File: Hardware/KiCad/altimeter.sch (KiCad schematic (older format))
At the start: 16 parts

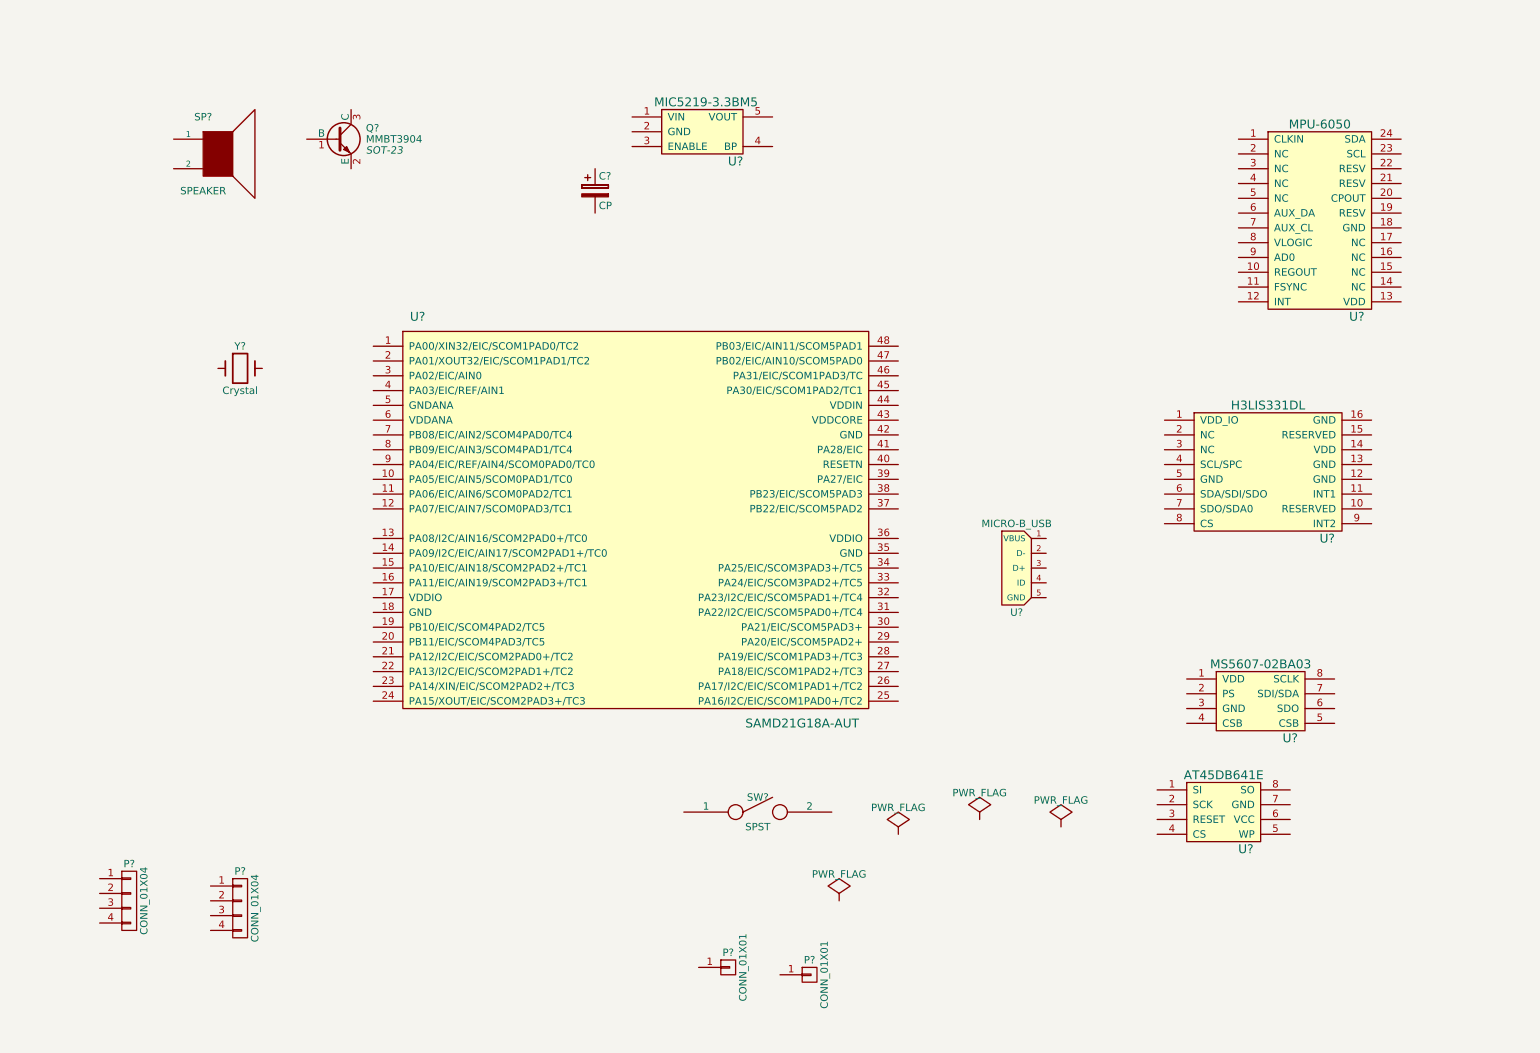
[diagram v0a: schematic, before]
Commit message: Pyro output, regulator and buzzer schematics created
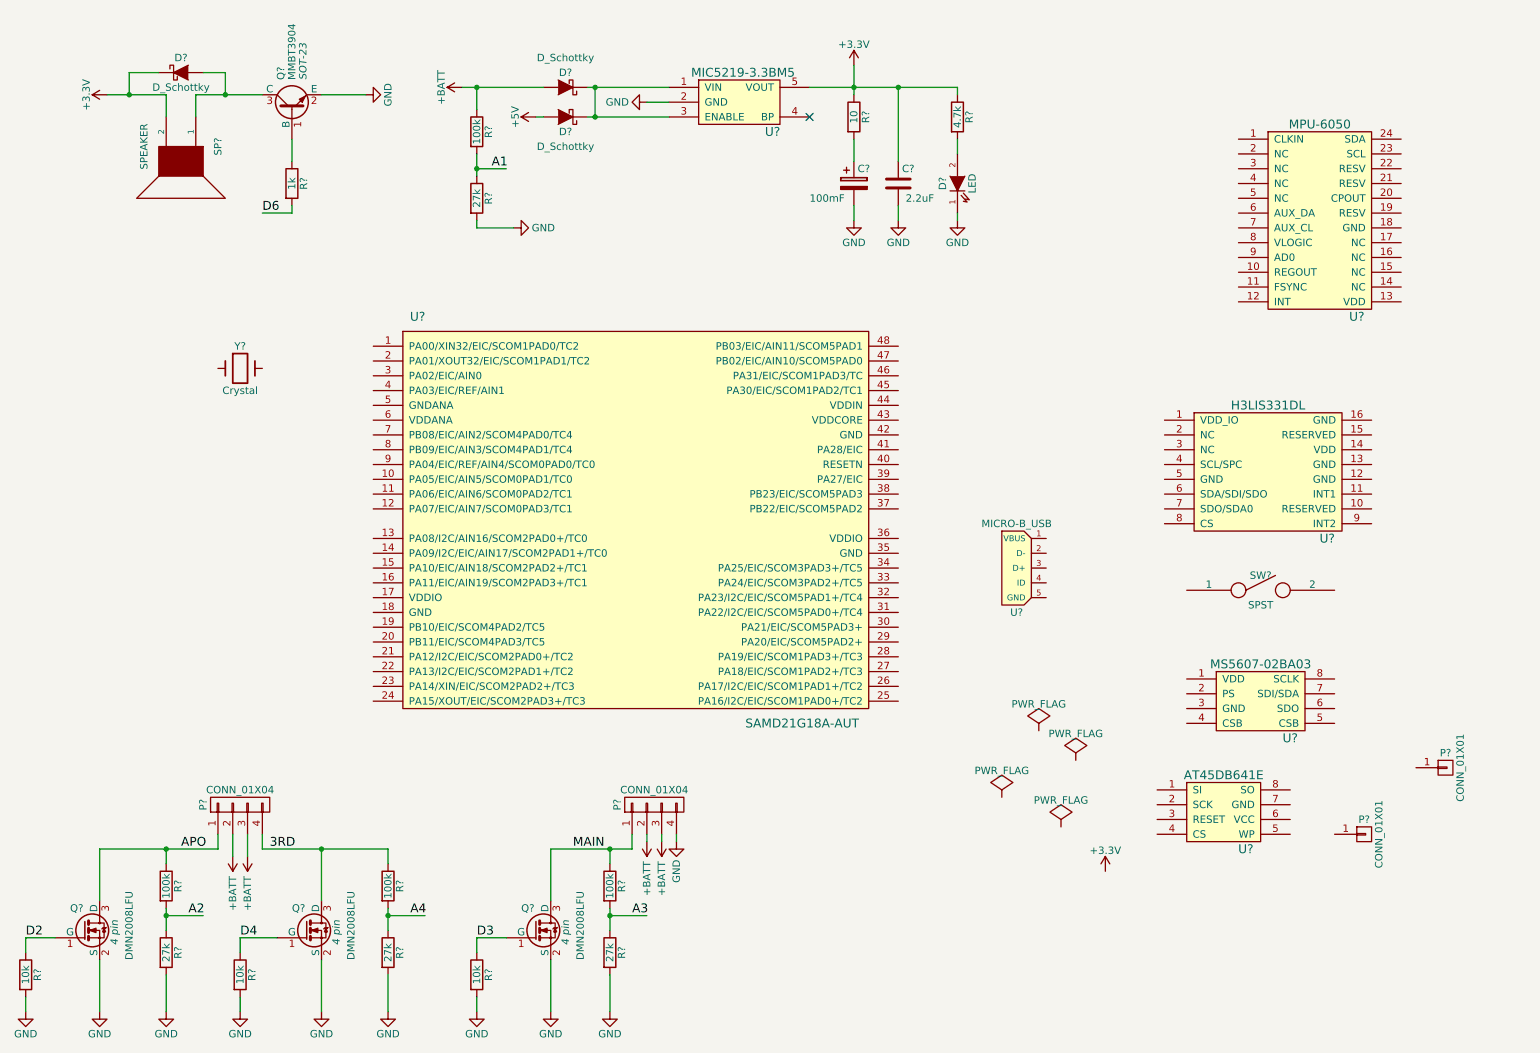
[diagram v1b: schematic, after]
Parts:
- removed P?: CONN_01X04, symbol CONN_01X04
- added C?: 2.2uF, symbol C
- added D? (x3): D_Schottky, symbol D_Schottky
- added D?: LED, symbol LED
- added P?: CONN_01X04, symbol CONN_01X04
- added Q? (x3): DMN2008LFU, 4 pin, symbol DMN2008LFU
- added R? (x4): 100k, symbol R
- added R? (x4): 27k, symbol R
- added R? (x3): 10k, symbol R
- added R?: 1k, symbol R
- added R?: 10, symbol R
- added R?: 4.7k, symbol R
- C?: value CP -> 100mF
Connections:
- net labels added: +3.3V, +5V, +BATT, 3RD, A1, A2, A3, A4, APO, D2, D3, D4, D6, GND, MAIN
- wire segments 0 -> 70
- no-connect marks 0 -> 1
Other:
- moved on the sheet: C?, P?, Q?, SP?, SW?, U?

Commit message: Schematic - sensors connected
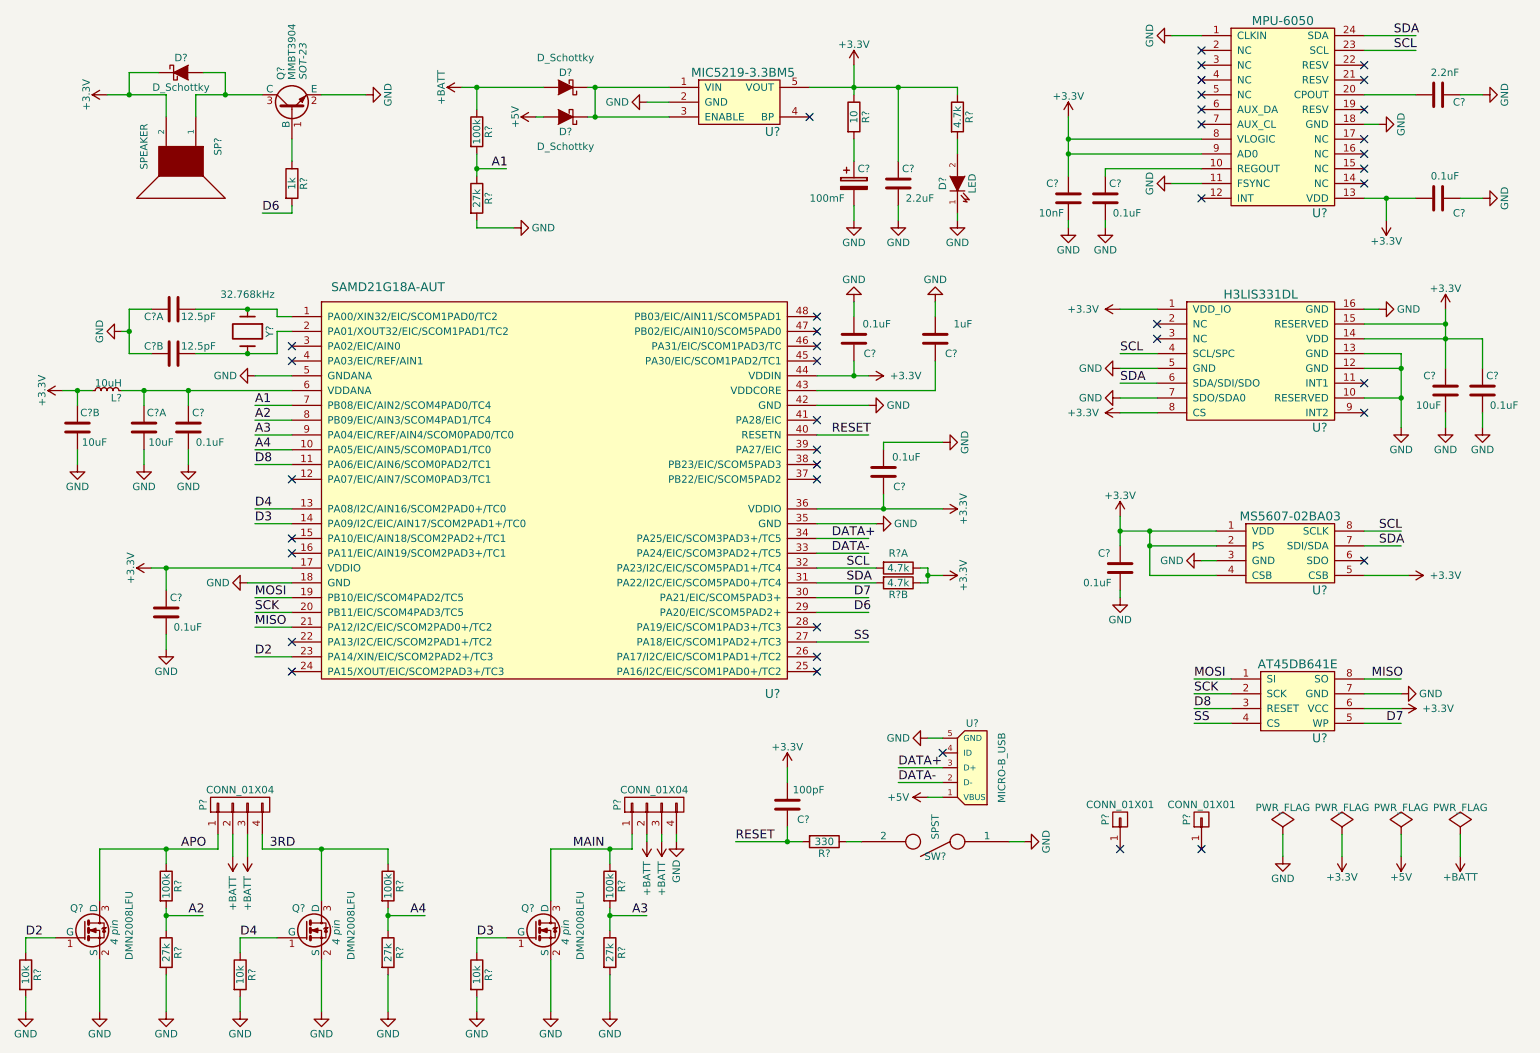
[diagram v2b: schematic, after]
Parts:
- removed Y?: Crystal, symbol Crystal
- added C?: 10nF, symbol C
- added C? (x8): 0.1uF, symbol C
- added C?: 2.2nF, symbol C
- added C?: 10uF, symbol C
- added C? (x2): 12.5pF, symbol C_2
- added C?: 1uF, symbol C
- added C? (x2): 10uF, symbol C_2
- added C?: 100pF, symbol C
- added L?: 10uH, symbol L
- added R? (x2): 4.7k, symbol R_2
- added R?: 330, symbol R
- added Y?: 32.768kHz, symbol Crystal
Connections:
- net labels added: D7, D8, DATA+, DATA-, MISO, MOSI, RESET, SCK, SCL, SDA, SS
- wire segments 70 -> 193
- no-connect marks 1 -> 41
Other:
- moved on the sheet: P?, SW?, U?

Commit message: combine resistors into arrays
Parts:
- removed D? (x3): D_Schottky, symbol D_Schottky
- removed Q?: MMBT3904, SOT-23, symbol MMBT3904
- removed R? (x4): 100k, symbol R
- removed R? (x4): 27k, symbol R
- removed R? (x3): 10k, symbol R
- removed R?: 1k, symbol R
- added D? (x3): Schottky_3, symbol Schottky_3
- added Q?: DMN2008LFU, 4 pin, symbol DMN2008LFU
- added R? (x4): 27k, symbol R_4
- added R? (x4): 100k, symbol R_4
- added R? (x4): 10k, symbol R_4
- R?: symbol R -> R_4
- R? (x2): symbol R_2 -> R_4
